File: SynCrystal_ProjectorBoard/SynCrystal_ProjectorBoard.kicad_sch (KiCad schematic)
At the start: 28 parts, among them J1 to TCA955 PCB, J2 to DIN connecting 3+1 Socket 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, J3 to Lamp Relay Board, J4 to DIN Socket traces, J5 Relais Board, J6 uC Cable, Q1 AO3400A, U1 AP63205WU, U2 LMC6482, U3 TS5A3160DBVR-TP, U4 TS5A3160DBVR-TP

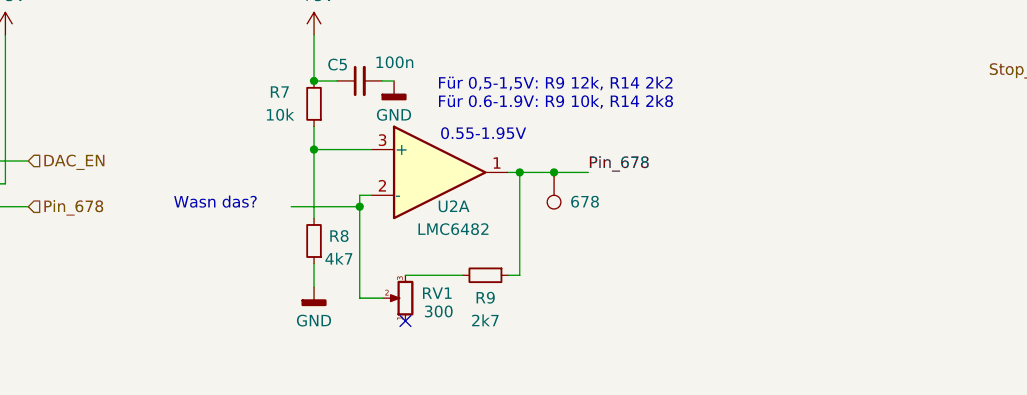
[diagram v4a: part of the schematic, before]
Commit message: Adding the OpAmp to the Projector Board, also, some LCSC Part numbers
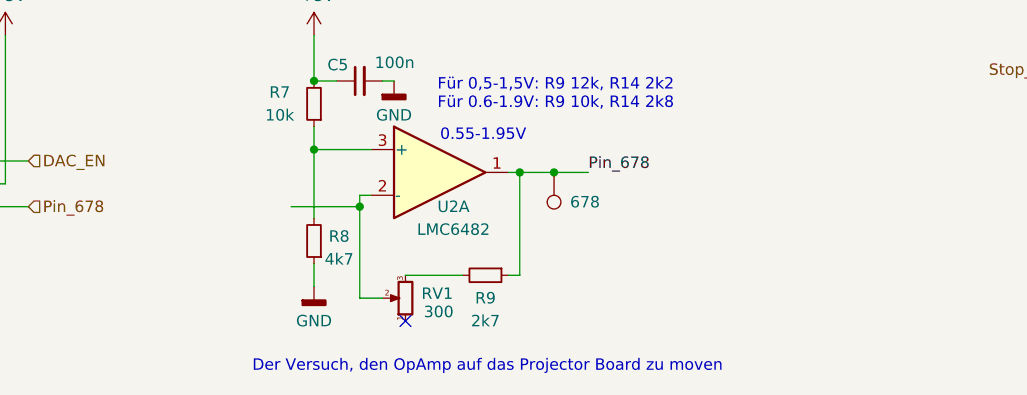
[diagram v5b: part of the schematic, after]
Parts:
- C1, C5: LCSC (none) -> C14663
- C2, C3: LCSC (none) -> C45783
- C4: LCSC (none) -> C15850
- R4, R9: LCSC (none) -> C13167
- R5, R6, R7: LCSC (none) -> C25804
- R8: LCSC (none) -> C23162
- RV1: footprint easyEDA:RES-SMD_RK10J11R0A0H -> easyEDA:RES-ADJ-SMD_3P-L3.8-W3.7_VGF39NCHXT; LCSC (none) -> C22461623
- U1: LCSC (none) -> C2071056
- U2: LCSC (none) -> C12620
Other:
- note added: "Der Versuch, den OpAmp auf das Projector Board zu moven"
- note removed: "Wasn das?"
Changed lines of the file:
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@@
 		)
 	)
-	(text "Wasn das?"
+	(text "Der Versuch, den OpAmp auf das Projector Board zu moven"
 		(exclude_from_sim no)
-		(at 124.968 134.366 0)
+		(at 129.032 152.4 0)
 		(effects
 			(font
 				(size 1.27 1.27)
 			)
+			(justify left)
 		)
 	)
@@
 			)
 		)
+		(property "LCSC" "C13167"
+			(at 154.94 142.24 0)
+			(effects
+				(font
+					(size 1.27 1.27)
+				)
+				(hide yes)
+			)
+		)
 		(pin "1"
 		)
@@
 			)
 		)
+		(property "LCSC" "C25804"
+			(at 135.89 123.19 0)
+			(effects
+				(font
+					(size 1.27 1.27)
+				)
+				(hide yes)
+			)
+		)
 		(pin "1"
 		)
@@
 			)
 		)
+		(property "LCSC" "C45783"
+			(at 156.21 31.75 0)
+			(effects
+				(font
+					(size 1.27 1.27)
+				)
+				(hide yes)
+			)
+		)
 		(pin "1"
 		)
@@
 			)
 		)
+		(property "LCSC" "C25804"
+			(at 246.38 124.46 0)
+			(effects
+				(font
+					(size 1.27 1.27)
+				)
+				(hide yes)
+			)
+		)
 		(pin "1"
 		)
@@
 			)
 		)
-		(property "Footprint" "easyEDA:RES-SMD_RK10J11R0A0H"
+		(property "Footprint" "easyEDA:RES-ADJ-SMD_3P-L3.8-W3.7_VGF39NCHXT"
 			(at 146.05 144.78 0)
 			(effects
@@
 			)
 		)
+		(property "LCSC" "C22461623"
+			(at 146.05 144.78 0)
+			(effects
+				(font
+					(size 1.27 1.27)
+				)
+				(hide yes)
+			)
+		)
 		(pin "2"
 		)
@@
 			)
 		)
+		(property "LCSC" "C13167"
+			(at 41.91 140.97 0)
+			(effects
+				(font
+					(size 1.27 1.27)
+				)
+				(hide yes)
+			)
+		)
 		(pin "1"
 		)
@@
 			)
 		)
+		(property "LCSC" "C14663"
+			(at 140.97 120.65 0)
+			(effects
+				(font
+					(size 1.27 1.27)
+				)
+				(hide yes)
+			)
+		)
 		(pin "1"
 		)
@@
 			)
 		)
+		(property "LCSC" "C15850"
+			(at 111.76 35.56 0)
+			(effects
+				(font
+					(size 1.27 1.27)
+				)
+				(hide yes)
+			)
+		)
 		(pin "1"
 		)
@@
 			)
 		)
+		(property "LCSC" "C45783"
+			(at 161.29 31.75 0)
+			(effects
+				(font
+					(size 1.27 1.27)
+				)
+				(hide yes)
+			)
+		)
 		(pin "1"
 		)
@@
 			)
 		)
+		(property "LCSC" "C23162"
+			(at 135.89 138.43 0)
+			(effects
+				(font
+					(size 1.27 1.27)
+				)
+				(hide yes)
+			)
+		)
 		(pin "1"
 		)
@@
 			)
 		)
+		(property "LCSC" "C25804"
+			(at 227.33 124.46 0)
+			(effects
+				(font
+					(size 1.27 1.27)
+				)
+				(hide yes)
+			)
+		)
 		(pin "1"
 		)
@@
 			)
 		)
+		(property "LCSC" "C14663"
+			(at 144.78 31.75 0)
+			(effects
+				(font
+					(size 1.27 1.27)
+				)
+				(hide yes)
+			)
+		)
 		(pin "1"
 		)
@@
 			)
 		)
+		(property "LCSC" "C12620"
+			(at 149.86 130.81 0)
+			(effects
+				(font
+					(size 1.27 1.27)
+				)
+				(hide yes)
+			)
+		)
 		(pin "8"
 		)
@@
 			(at 130.81 34.29 0)
 			(effects
+				(font
+					(size 1.27 1.27)
+				)
+				(hide yes)
+			)
+		)
+		(property "LCSC" "C2071056"
+			(at 130.81 34.29 0)
+			(effects

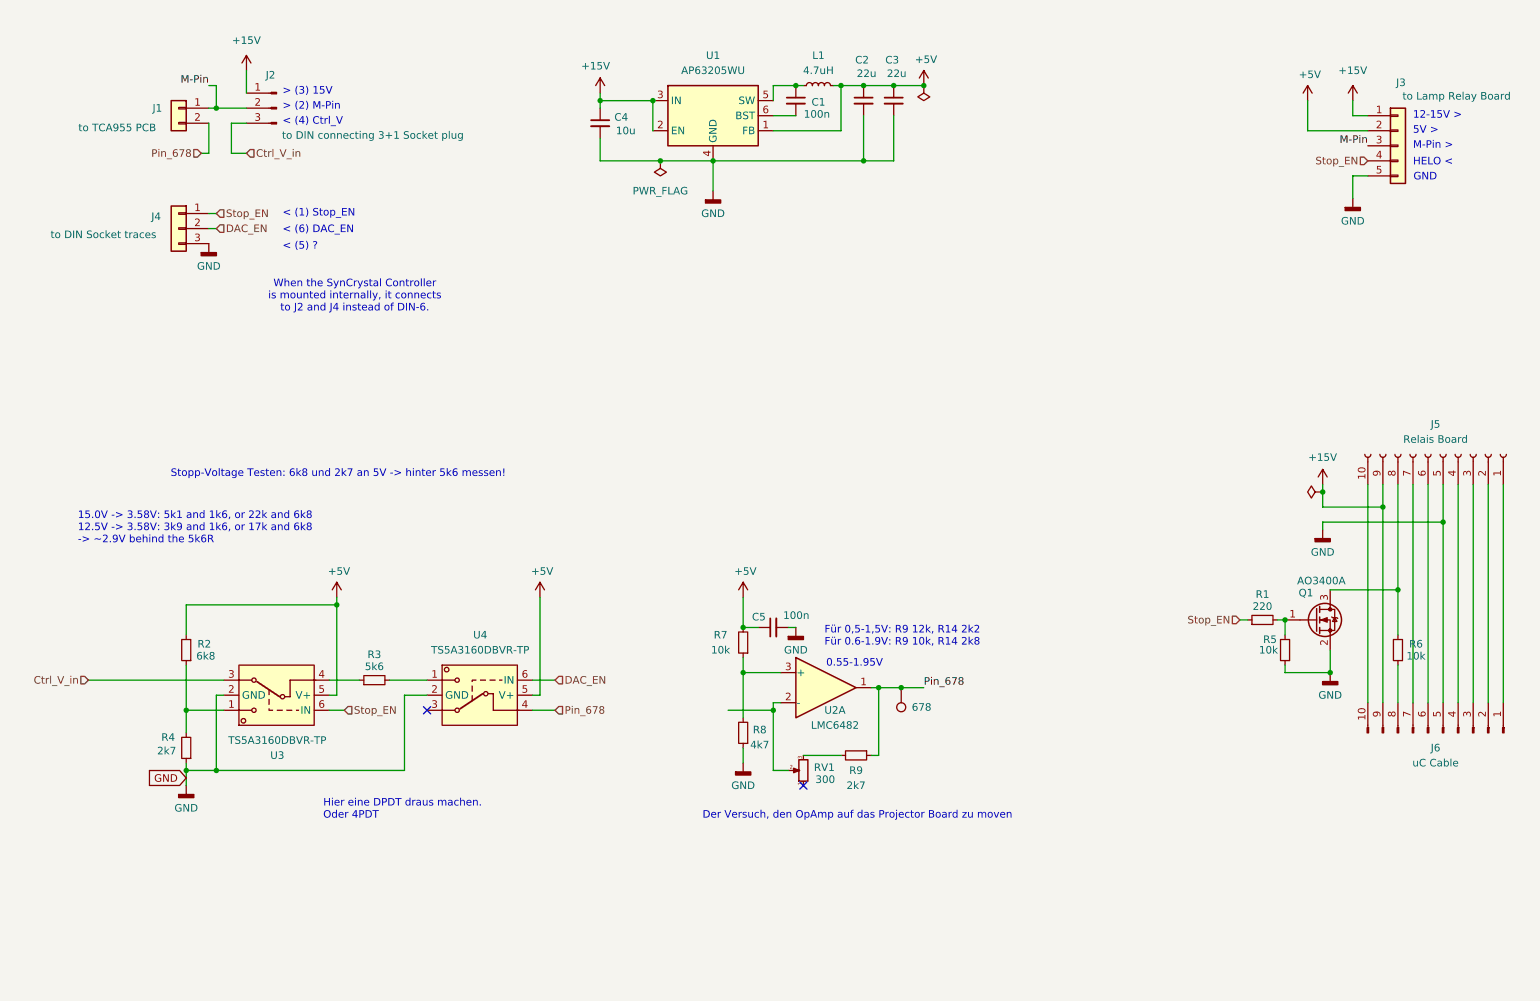
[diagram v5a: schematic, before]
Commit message: Moved the OpAmp to the Projector Board. This Layout is DRC 0, but not optimal
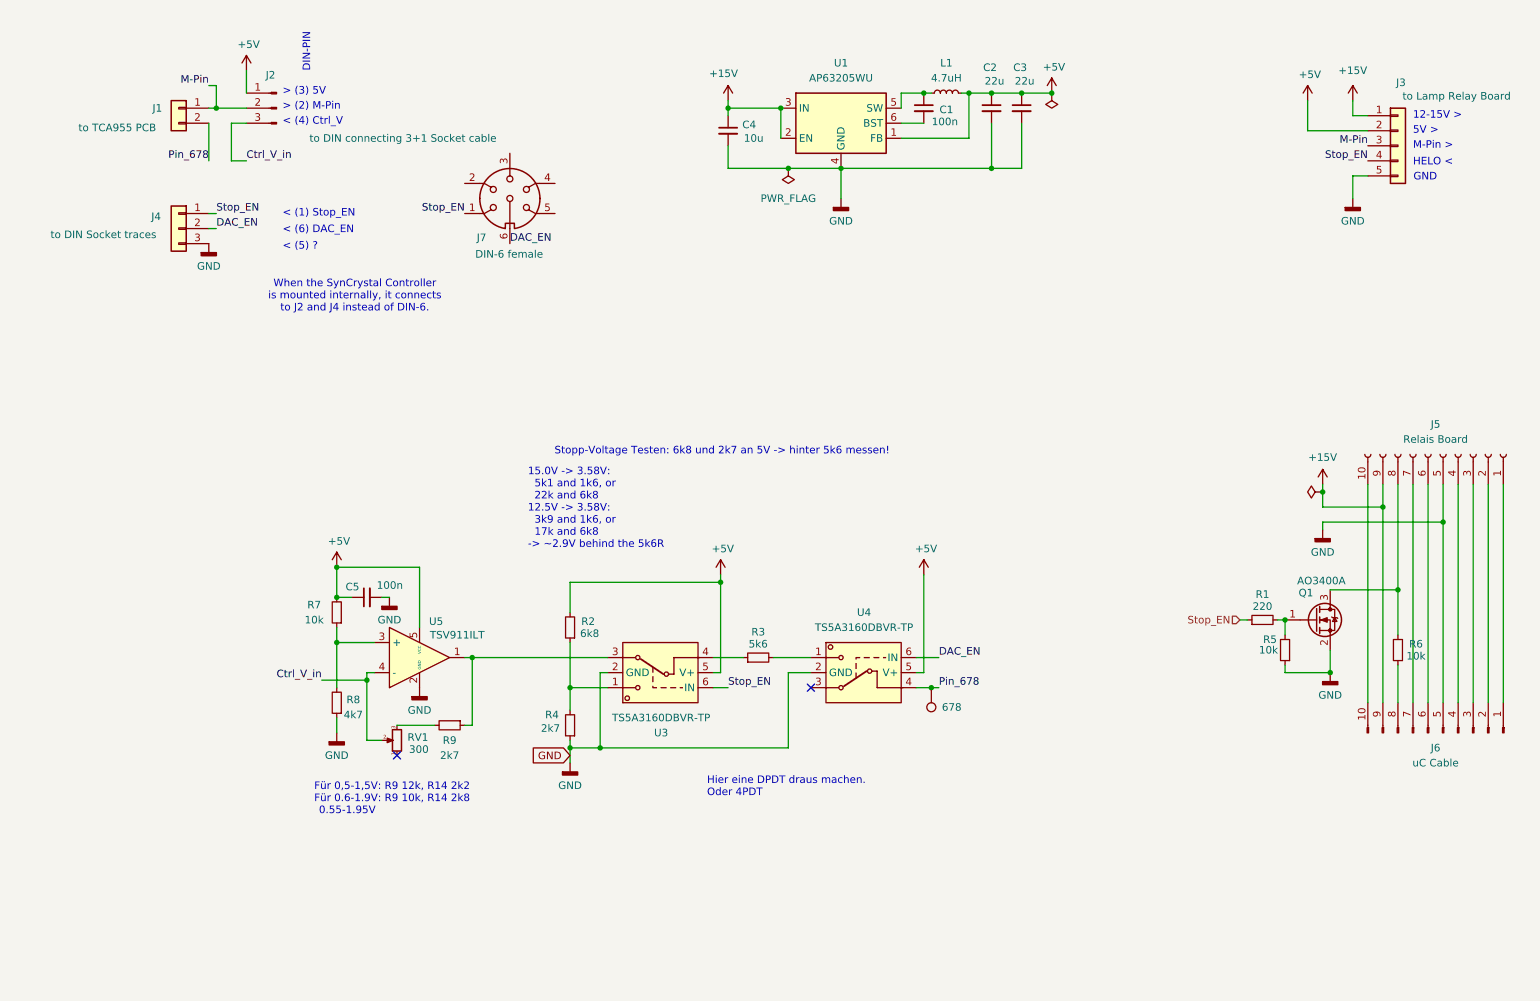
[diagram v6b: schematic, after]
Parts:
- removed U2: LMC6482, Package_SO:SOIC-8_3.9x4.9mm_P1.27mm, symbol Amplifier_Operational:LMC6482
- added J7: DIN-6 female, symbol Connector:DIN-6
- added U5: TSV911ILT, easyEDA:SOT-23-5_L2.9-W1.6-P0.95-LS2.8-BR, symbol easyEDA:TSV911ILT
- J2: value to DIN connecting 3+1 Socket plug -> to DIN connecting 3+1 Socket cable
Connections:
- net +15V: no longer J2.1 (Pin_1)
- net +5V: now also J2.1 (Pin_1), U5.5 (VCC)
- net Ctrl_V_in: now also RV1.2, U5.4 (-); no longer U3.3
- net DAC_EN: now also J7.6
- net GND: now also U5.2 (GND)
- net Pin_678: no longer R9.1
- net Stop_EN: now also J7.1
- net at R7.1, R8.2: now also U5.3 (+)
- new net: R9.1, U3.3, U5.1
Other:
- note added: "> (3) 5V"
- note added: "DIN-PIN"
- note removed: "> (3) 15V"
- note removed: "Der Versuch, den OpAmp auf das Projector Board zu moven"
- moved on the sheet: C1, C2, C3, C4, C5, L1, R2, R3, R4, R7, R8, R9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

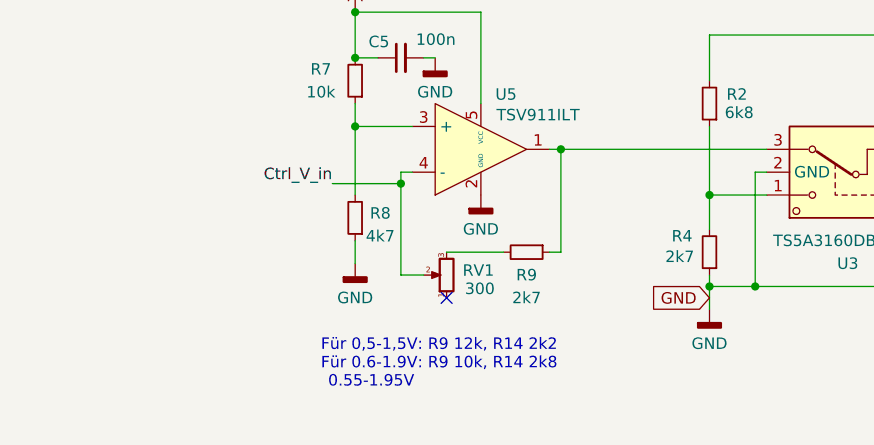
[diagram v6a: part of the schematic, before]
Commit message: moving the 10k OpAmp Input R to the Projector board
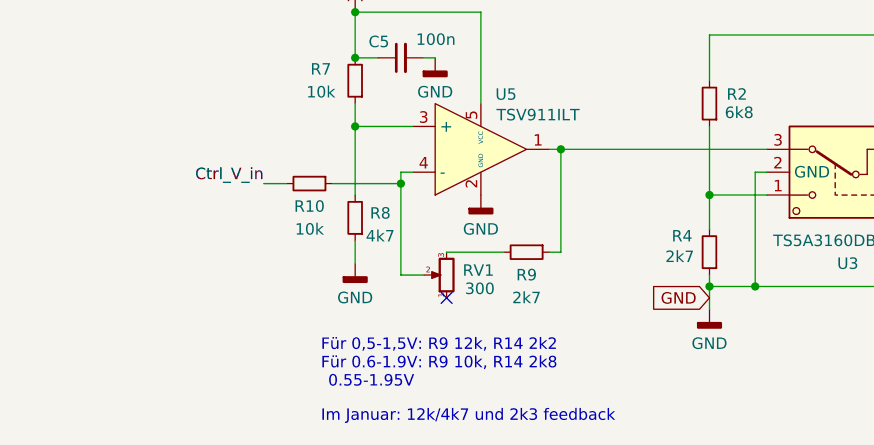
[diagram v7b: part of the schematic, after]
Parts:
- added R10: 10k, Resistor_SMD:R_0603_1608Metric, symbol Device:R_Small
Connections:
- net Ctrl_V_in: now also R10.2; no longer RV1.2, U5.4 (-)
- new net: R10.1, RV1.2, U5.4 (-)
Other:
- note added: "Im Januar: 12k/4k7 und 2k3 feedback"
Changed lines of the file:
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@@
 	(wire
 		(pts
+			(xy 57.15 129.54) (xy 59.69 129.54)
+		)
+		(stroke
+			(width 0)
+			(type default)
+		)
+	)
+	(wire
+		(pts
 			(xy 133.35 39.37) (xy 133.35 43.18)
 		)
@@
 		)
 	)
+	(text "Im Januar: 12k/4k7 und 2k3 feedback"
+		(exclude_from_sim no)
+		(at 63.5 155.448 0)
+		(effects
+			(font
+				(size 1.27 1.27)
+			)
+			(justify left)
+		)
+	)
 	(text "> (2) M-Pin"
 		(exclude_from_sim no)
@@
 	)
 	(label "Ctrl_V_in"
-		(at 64.77 129.54 180)
+		(at 57.15 129.54 180)
 		(effects
 			(font
@@
 					(unit 1)
 				)
+			)
+		)
+	)
+	(symbol
+		(lib_id "Device:R_Small")
+		(at 62.23 129.54 270)
+		(unit 1)
+		(exclude_from_sim no)
+		(in_bom yes)
+		(on_board yes)
+		(dnp no)
+		(property "Reference" "R10"
+			(at 62.23 132.08 90)
+			(effects
+				(font
+					(size 1.27 1.27)
+				)
+			)
+		)
+		(property "Value" "10k"
+			(at 62.23 134.62 90)
+			(effects
+				(font
+					(size 1.27 1.27)
+				)
+			)
+		)
+		(property "Footprint" "Resistor_SMD:R_0603_1608Metric"
+			(at 62.23 129.54 0)
+			(effects
+				(font
+					(size 1.27 1.27)
+				)
+				(hide yes)
+			)
+		)
+		(property "Datasheet" "~"
+			(at 62.23 129.54 0)
+			(effects
+				(font
+					(size 1.27 1.27)
+				)
+				(hide yes)
+			)
+		)
+		(property "Description" ""
+			(at 62.23 129.54 0)
+			(effects
+				(font
+					(size 1.27 1.27)
+				)
+				(hide yes)
+			)
+		)
+		(property "LCSC" "C25804"
+			(at 62.23 129.54 0)
+			(effects
+				(font
+					(size 1.27 1.27)
+				)
+				(hide yes)
+			)
+		)
+		(pin "1"
+		)
+		(pin "2"
+		)
+		(instances
+			(project "SynCrystal_ProjectorBoard"
+				(path "/01bd7818-adef-4612-bb26-3dbff95808f6"
+					(reference "R10")
+					(unit 1)
+				)

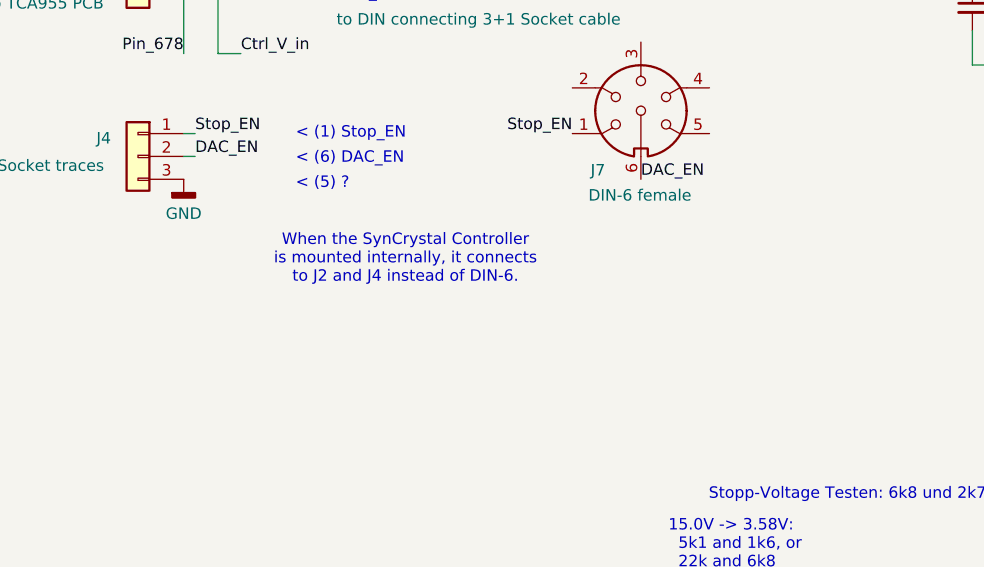
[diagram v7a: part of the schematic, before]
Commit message: Adding the VOltage Divider to Projector Board to allow Projector Detection. Also, fixing various footprints on the controller. ERC now failing.
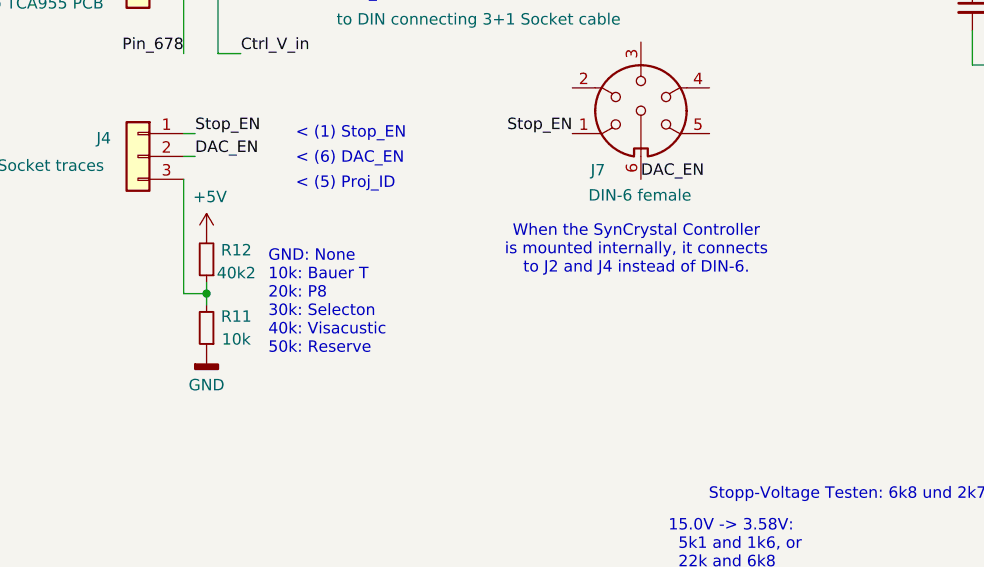
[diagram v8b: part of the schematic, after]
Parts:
- added R11: 10k, Resistor_SMD:R_0402_1005Metric, symbol Device:R_Small
- added R12: 40k2, Resistor_SMD:R_0402_1005Metric, symbol Device:R_Small
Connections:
- net +5V: now also R12.2
- net GND: now also R11.1; no longer J4.3 (Pin_3)
- new net: J4.3 (Pin_3), R11.2, R12.1
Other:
- note added: "< (5) Proj_ID"
- note added: "GND: None 10k: Bauer T 20k: P8 30k: Selecton 40k: Visacustic 50k: Reserve"
- note removed: "< (5) ?"
